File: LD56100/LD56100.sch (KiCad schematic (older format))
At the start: 3 parts, among them J1 Conn_01x04_Male, J2 Conn_01x04_Male, U1 LD56100

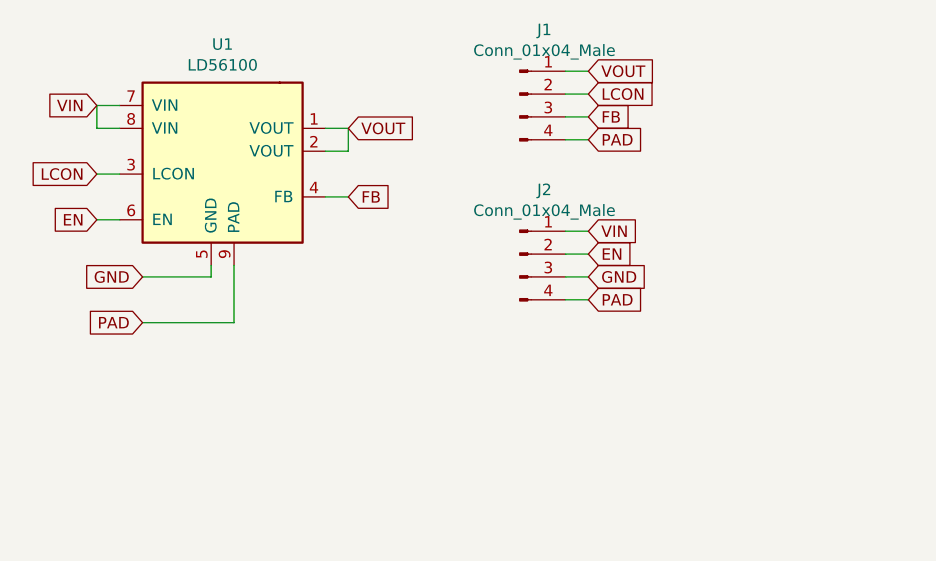
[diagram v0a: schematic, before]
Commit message: build the gerbers for the LD56100, and build SOT-363
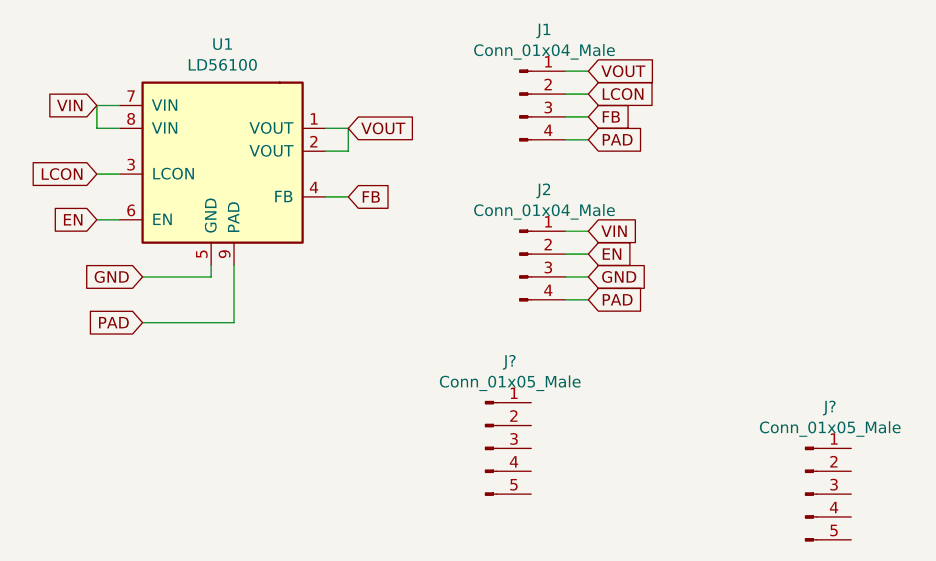
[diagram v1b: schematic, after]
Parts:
- added J? (x2): Conn_01x05_Male, symbol Connector:Conn_01x05_Male
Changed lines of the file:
@@
-	1    0    0    -1
-$EndComp
-$Comp
-L Connector:Conn_01x04_Male J1
-U 1 1 5F1CE35D
-P 6550 3150
-F 0 "J1" H 6658 3431 50  0000 C CNN
-F 1 "Conn_01x04_Male" H 6658 3340 50  0000 C CNN
-F 2 "Connector_PinSocket_2.54mm:PinSocket_1x04_P2.54mm_Vertical" H 6550 3150 50  0001 C CNN
-F 3 "~" H 6550 3150 50  0001 C CNN
-	1    6550 3150
 	1    0    0    -1
 $EndComp
@@
 Wire Wire Line
 	5300 4150 5300 3900
-$Comp
-L Connector:Conn_01x04_Male J2
-U 1 1 5F1D345D
-P 6550 3850
-F 0 "J2" H 6658 4131 50  0000 C CNN
-F 1 "Conn_01x04_Male" H 6658 4040 50  0000 C CNN
-F 2 "Connector_PinSocket_2.54mm:PinSocket_1x04_P2.54mm_Vertical" H 6550 3850 50  0001 C CNN
-F 3 "~" H 6550 3850 50  0001 C CNN
-	1    6550 3850
-	1    0    0    -1
-$EndComp
 Text GLabel 6850 3050 2    50   Input ~ 0
 VOUT
@@
 Wire Wire Line
 	6750 4050 6850 4050
+$Comp
+L Connector:Conn_01x05_Male J?
+U 1 1 5F2B934A
+P 7800 4900
+F 0 "J?" H 7908 5281 50  0000 C CNN
+F 1 "Conn_01x05_Male" H 7908 5190 50  0000 C CNN
+F 2 "" H 7800 4900 50  0001 C CNN
+F 3 "~" H 7800 4900 50  0001 C CNN
+	1    7800 4900
+	1    0    0    -1
+$EndComp
+$Comp
+L Connector:Conn_01x04_Male J1
+U 1 1 5F1CE35D
+P 6550 3150
+F 0 "J1" H 6658 3431 50  0000 C CNN
+F 1 "Conn_01x04_Male" H 6658 3340 50  0000 C CNN
+F 2 "Connector_PinSocket_2.54mm:PinSocket_1x04_P2.54mm_Vertical" H 6550 3150 50  0001 C CNN
+F 3 "~" H 6550 3150 50  0001 C CNN
+	1    6550 3150
+	1    0    0    -1
+$EndComp
+$Comp
+L Connector:Conn_01x05_Male J?
+U 1 1 5F2B8C85
+P 6400 4700
+F 0 "J?" H 6508 5081 50  0000 C CNN
+F 1 "Conn_01x05_Male" H 6508 4990 50  0000 C CNN
+F 2 "" H 6400 4700 50  0001 C CNN
+F 3 "~" H 6400 4700 50  0001 C CNN
+	1    6400 4700
+	1    0    0    -1
+$EndComp
+$Comp
+L Connector:Conn_01x04_Male J2
+U 1 1 5F1D345D
+P 6550 3850
+F 0 "J2" H 6658 4131 50  0000 C CNN
+F 1 "Conn_01x04_Male" H 6658 4040 50  0000 C CNN
+F 2 "Connector_PinSocket_2.54mm:PinSocket_1x04_P2.54mm_Vertical" H 6550 3850 50  0001 C CNN
+F 3 "~" H 6550 3850 50  0001 C CNN
+	1    6550 3850
+	1    0    0    -1
+$EndComp
 $EndSCHEMATC
